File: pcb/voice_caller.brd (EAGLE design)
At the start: 52.4 x 59.1 mm, 48 parts, among them IC1 PRO_MICRO, IC2 LM386M-1, IC3 78L12SMD, K1 TQ2SA-L2-5V, U1 25F32006WSOI

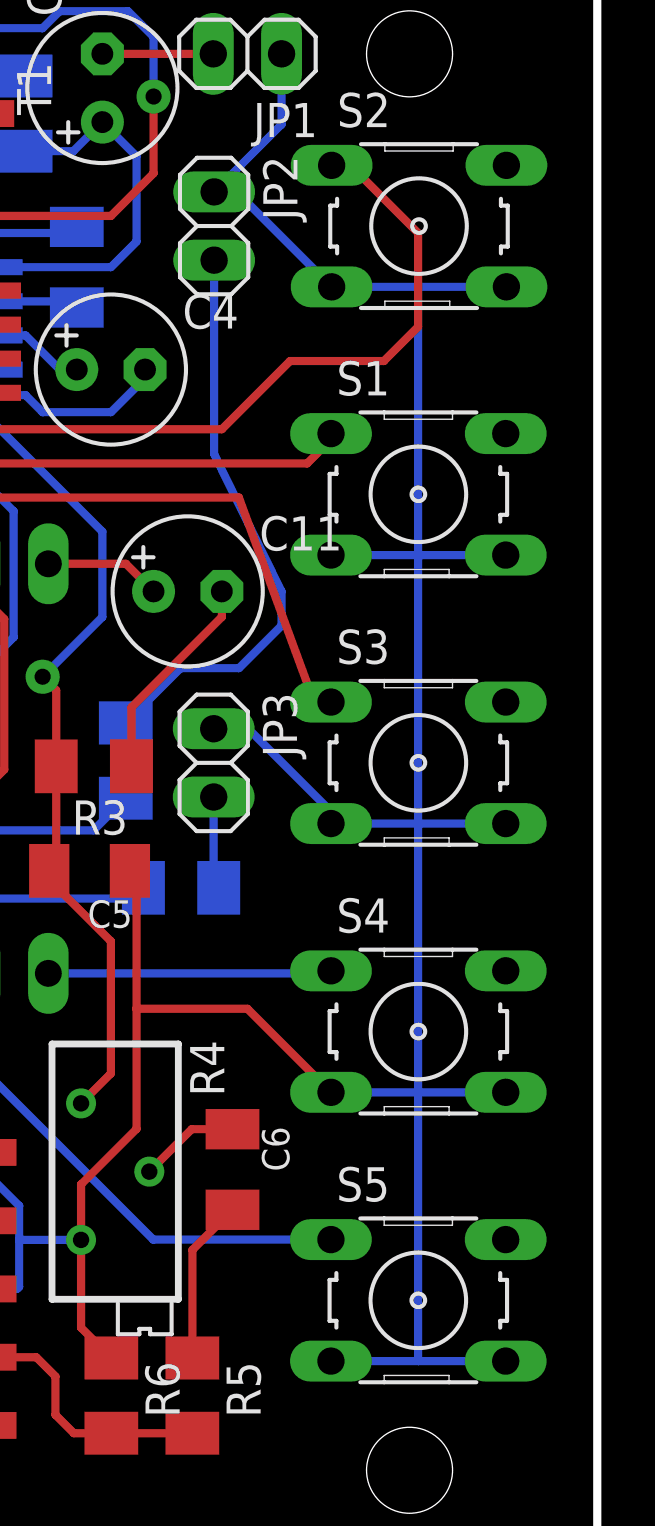
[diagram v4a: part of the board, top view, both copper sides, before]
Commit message: Filter capacitors added to pushbuttons
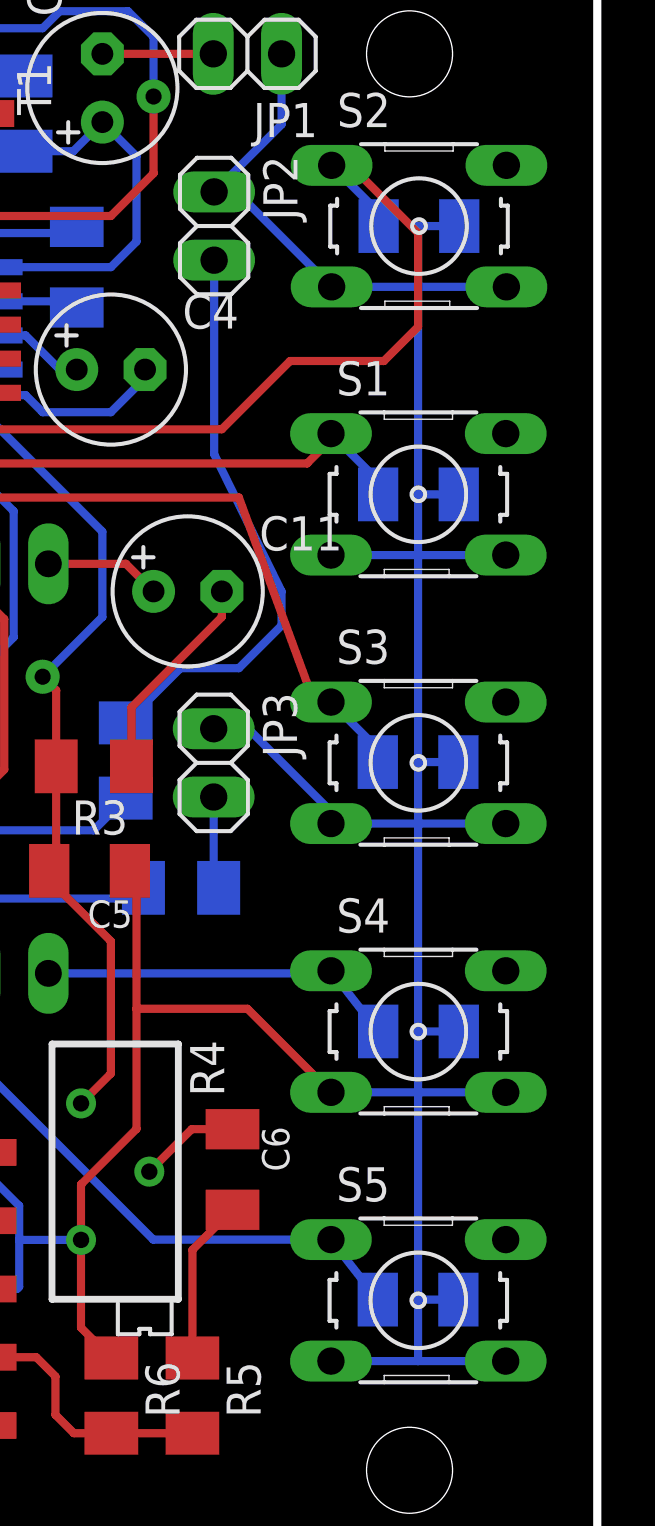
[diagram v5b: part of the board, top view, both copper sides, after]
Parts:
- added C13, C14, C15, C16, C17: 10nF, rcl:C1206K
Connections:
- net BUTTON1: now also C16.1
- net BUTTON2: now also C17.1
- net BUTTON3: now also C13.1
- net BUTTON4: now also C14.1
- net BUTTON5: now also C15.1
- net GND: now also C13.2, C14.2, C15.2, C16.2, C17.2
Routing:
- net GND: track 320.6 -> 330.5 mm
- net BUTTON2: track 29.2 -> 32.2 mm
- net BUTTON1: track 43.8 -> 46.8 mm
- net BUTTON3: track 28.0 -> 31.0 mm
- net BUTTON4: track 10.6 -> 13.4 mm
- net BUTTON5: track 19.2 -> 22.0 mm
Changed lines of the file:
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@@
 <element name="C12" library="rcl" package="C1206K" value="100nF" x="31.115" y="36.5125" rot="MR180"/>
 <element name="D1" library="diode" package="SOD80C" value="" x="30.1625" y="39.37" rot="MR180"/>
+<element name="C13" library="rcl" package="C1206K" value="10nF" x="56.1975" y="35.2425" rot="MR180"/>
+<element name="C14" library="rcl" package="C1206K" value="10nF" x="56.21264375" y="25.218809375" rot="MR180"/>
+<element name="C15" library="rcl" package="C1206K" value="10nF" x="56.1975" y="15.24" rot="MR180"/>
+<element name="C16" library="rcl" package="C1206K" value="10nF" x="56.22905" y="55.187159375" rot="MR180"/>
+<element name="C17" library="rcl" package="C1206K" value="10nF" x="56.21109375" y="45.2026625" rot="MR180"/>
 </elements>
 <signals>
@@
 <wire x1="45.72" y1="21.59" x2="43.65625" y2="19.52625" width="0.3048" layer="1"/>
 <wire x1="43.65625" y1="19.52625" x2="43.65625" y2="17.4625" width="0.3048" layer="1"/>
-<wire x1="56.1975" y1="52.925025" x2="56.1975" y2="42.943775" width="0.3048" layer="16"/>
-<wire x1="56.1975" y1="42.943775" x2="56.1975" y2="32.953740625" width="0.3048" layer="16"/>
-<wire x1="56.1975" y1="32.953740625" x2="56.1975" y2="22.953740625" width="0.3048" layer="16"/>
-<wire x1="56.1975" y1="22.953740625" x2="56.1975" y2="12.95254375" width="0.3048" layer="16"/>
+<wire x1="56.1975" y1="52.925025" x2="56.1975" y2="45.085" width="0.3048" layer="16"/>
+<wire x1="56.1975" y1="45.085" x2="56.1975" y2="42.943775" width="0.3048" layer="16"/>
+<wire x1="56.1975" y1="42.943775" x2="56.1975" y2="35.2425" width="0.3048" layer="16"/>
+<wire x1="56.1975" y1="35.2425" x2="56.1975" y2="32.953740625" width="0.3048" layer="16"/>
+<wire x1="56.1975" y1="32.953740625" x2="56.1975" y2="25.218809375" width="0.3048" layer="16"/>
+<wire x1="56.1975" y1="25.218809375" x2="56.1975" y2="22.953740625" width="0.3048" layer="16"/>
+<wire x1="56.1975" y1="22.953740625" x2="56.1975" y2="15.24" width="0.3048" layer="16"/>
+<wire x1="56.1975" y1="15.24" x2="56.1975" y2="12.95254375" width="0.3048" layer="16"/>
 <wire x1="30.8375" y1="49.2525" x2="30.8375" y2="49.38875" width="0.4064" layer="1"/>
 <wire x1="28.11625" y1="49.38875" x2="30.8375" y2="49.38875" width="0.3048" layer="1"/>
@@
 <wire x1="29.615" y1="36.5125" x2="28.4625" y2="37.665" width="0.3048" layer="16"/>
 <wire x1="28.4625" y1="37.665" x2="28.4625" y2="39.37" width="0.3048" layer="16"/>
+<contactref element="C13" pad="2"/>
+<contactref element="C14" pad="2"/>
+<contactref element="C15" pad="2"/>
+<contactref element="C16" pad="2"/>
+<contactref element="C17" pad="2"/>
+<wire x1="57.71109375" y1="45.2026625" x2="56.3151625" y2="45.2026625" width="0.3048" layer="16"/>
+<wire x1="56.3151625" y1="45.2026625" x2="56.1975" y2="45.085" width="0.3048" layer="16"/>
+<wire x1="57.6975" y1="35.2425" x2="56.1975" y2="35.2425" width="0.3048" layer="16"/>
+<wire x1="57.72905" y1="55.187159375" x2="56.1975" y2="55.187159375" width="0.3048" layer="16"/>
+<wire x1="56.1975" y1="55.187159375" x2="56.1975" y2="52.925025" width="0.3048" layer="16"/>
+<wire x1="57.71264375" y1="25.218809375" x2="56.1975" y2="25.218809375" width="0.3048" layer="16"/>
+<wire x1="57.6975" y1="15.24" x2="56.1975" y2="15.24" width="0.3048" layer="16"/>
 </signal>
 <signal name="MOSI">
@@
 <wire x1="27.2" y1="42.62" x2="27.2" y2="44.345" width="0.3048" layer="1"/>
 <wire x1="27.2" y1="44.345" x2="29.21" y2="46.355" width="0.3048" layer="1"/>
+<contactref element="C17" pad="1"/>
+<wire x1="54.71109375" y1="45.2026625" x2="54.71109375" y2="45.71143125" width="0.3048" layer="16"/>
+<wire x1="54.71109375" y1="45.71143125" x2="52.95755" y2="47.464975" width="0.3048" layer="16"/>
 </signal>
 <signal name="BUTTON1">
@@
 <wire x1="53.6575" y1="57.4675" x2="53.002575" y2="57.4675" width="0.3048" layer="1"/>
 <wire x1="53.002575" y1="57.4675" x2="52.9813" y2="57.446225" width="0.3048" layer="1"/>
+<contactref element="C16" pad="1"/>
+<wire x1="54.72905" y1="55.187159375" x2="54.72905" y2="55.698475" width="0.3048" layer="16"/>
+<wire x1="54.72905" y1="55.698475" x2="52.9813" y2="57.446225" width="0.3048" layer="16"/>
 </signal>
 <signal name="PTT_SENSE">
@@
 <wire x1="52.332175" y1="37.465" x2="52.94729375" y2="37.465" width="0.3048" layer="1"/>
 <wire x1="52.94729375" y1="37.465" x2="52.957234375" y2="37.474940625" width="0.3048" layer="1"/>
+<contactref element="C13" pad="1"/>
+<wire x1="54.6975" y1="35.2425" x2="54.6975" y2="35.734675" width="0.3048" layer="16"/>
+<wire x1="54.6975" y1="35.734675" x2="52.957234375" y2="37.474940625" width="0.3048" layer="16"/>
 </signal>
 <signal name="BUTTON5">
@@
 <wire x1="46.34375625" y1="17.47374375" x2="39.9" y2="23.9175" width="0.3048" layer="16"/>
 <wire x1="39.9" y1="23.9175" x2="39.9" y2="27.38" width="0.3048" layer="16"/>
+<contactref element="C15" pad="1"/>
+<wire x1="54.6975" y1="15.24" x2="52.954765625" y2="17.47374375" width="0.3048" layer="16"/>
 </signal>
 <signal name="BUTTON4">
@@
 <wire x1="42.44" y1="27.38" x2="52.86229375" y2="27.38" width="0.3048" layer="16"/>
 <wire x1="52.86229375" y1="27.38" x2="52.957234375" y2="27.474940625" width="0.3048" layer="16"/>
+<contactref element="C14" pad="1"/>
+<wire x1="54.71264375" y1="25.218809375" x2="52.957234375" y2="27.474940625" width="0.3048" layer="16"/>
 </signal>
 <signal name="PTT_SW">

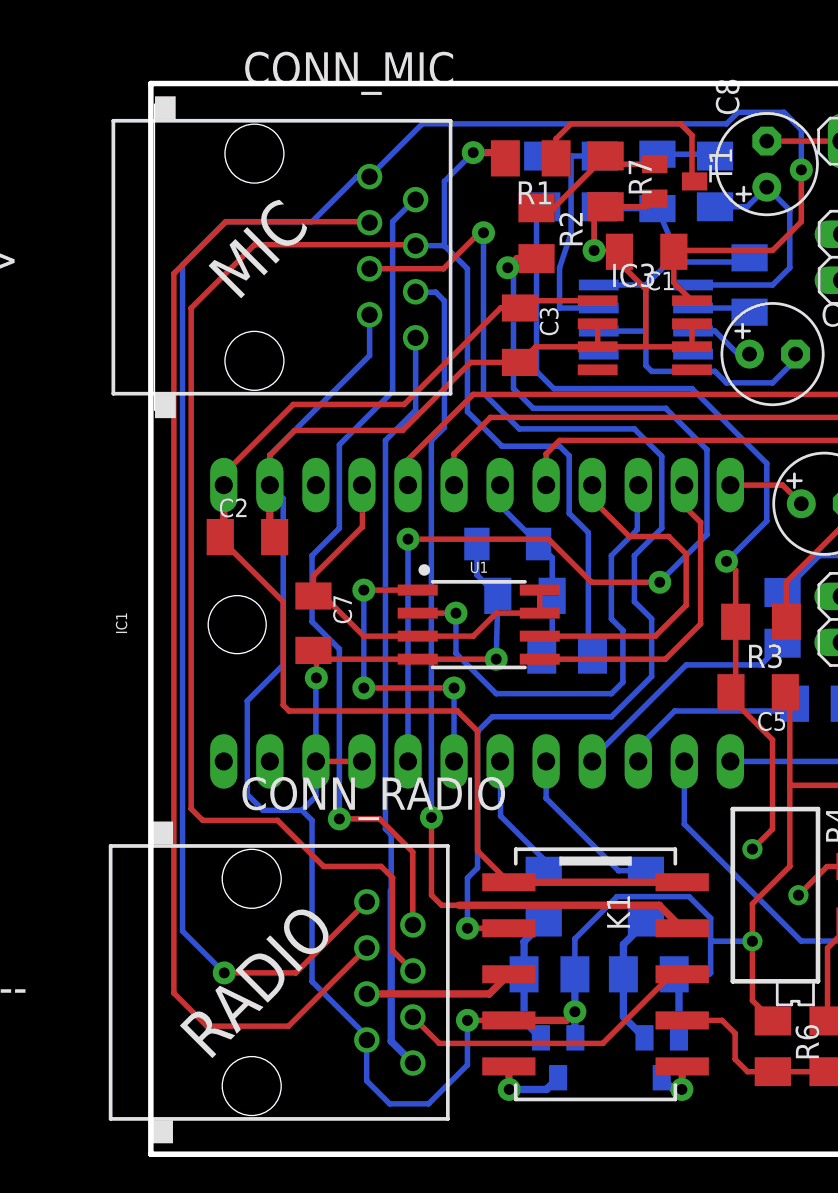
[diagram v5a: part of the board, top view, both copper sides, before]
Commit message: RJ-45 connectors moves 1.3mm inwards.
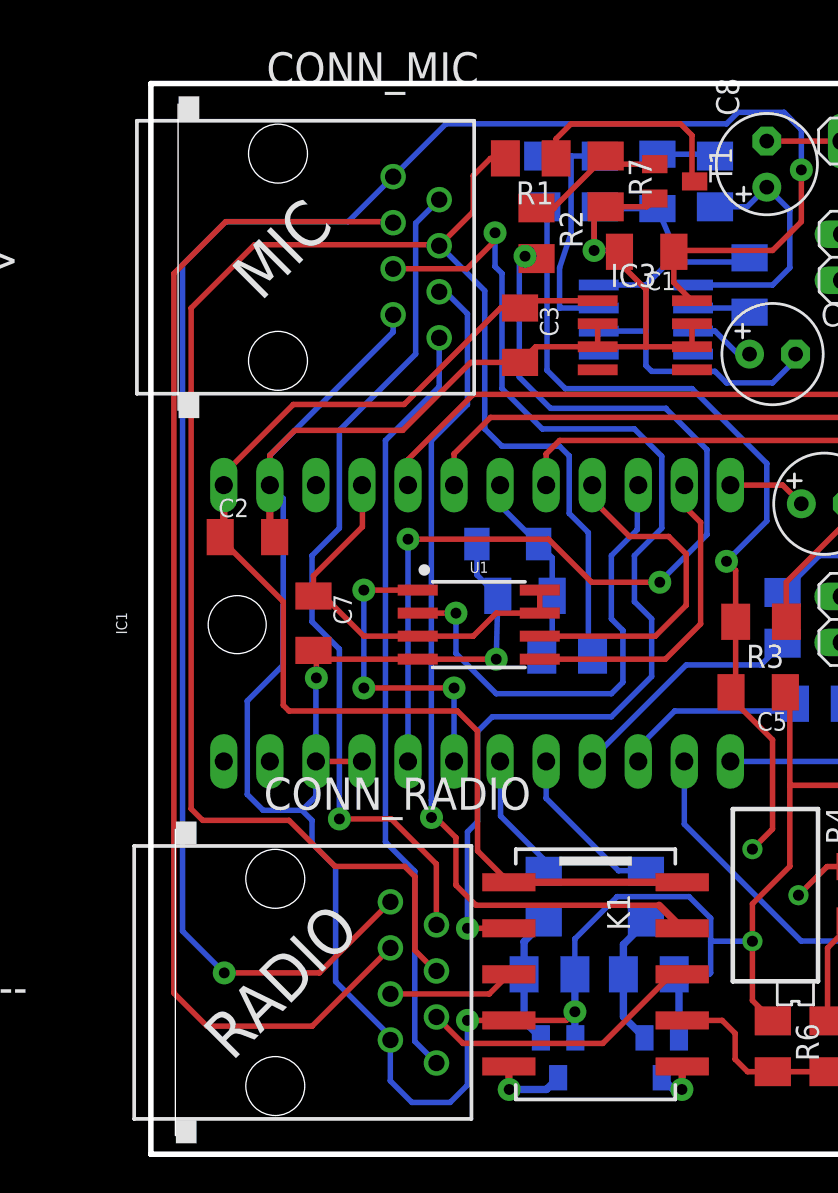
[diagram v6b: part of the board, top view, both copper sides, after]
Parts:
- moved CONN_RADIO 1.30 mm to (17.3, 15.2)
- moved CONN_MIC 1.30 mm to (17.5, 55.2)
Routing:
- net AF_OUT: track 64.9 -> 67.5 mm
- net FREQ_UD: track 46.0 -> 47.4 mm
- net MIC_GND: track 64.6 -> 63.2 mm
- net +8V: track 103.4 -> 104.7 mm
- net MIC_RADIO: track 17.0 -> 15.7 mm
- net MIC_GND_RADIO: track 8.28 -> 6.98 mm
- net PTT_SW: track 56.2 -> 55.1 mm
- net SQUELCH: track 41.3 -> 42.4 mm
- net MIC: track 49.5 -> 48.6 mm
- net PTT: track 96.9 -> 97.6 mm, vias 1 -> 0

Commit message: Final adjustments.
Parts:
- removed JP1, JP2, JP3: (no value), pinhead:1X02
- removed K1: TQ2SA-L2-5V, relay:TQ-SA
- removed U1: 25F32006WSOI, SparkFun-IC-Memory:SO08-EIAJ
- added ARDUINO: PRO_MICRO, SparkFun-Boards:SPARKFUN_PRO_MICRO
- added LED1, LED2, SPK: (no value), pinhead:1X02
- added RLY1: TQ2SA-L2-5V, relay:TQ-SA
- IC1: value PRO_MICRO -> 78L12SMD; device SparkFun-Boards:SPARKFUN_PRO_MICRO -> linear:SO08
- IC3: value 78L12SMD -> 25F32006WSOI; device linear:SO08 -> SparkFun-IC-Memory:SO08-EIAJ
- moved IC3 56.4 mm to (13.3, 0.00)
- moved S2 47.8 mm to (40.6, 9.96)
- moved C16 38.5 mm to (40.6, 19.9)
- moved C14 38.5 mm to (40.6, -10.0)
- moved C17 38.5 mm to (40.6, 9.96)
- moved S3 38.5 mm to (40.6, -0.03)
- moved S4 38.5 mm to (40.6, -10.0)
- moved S5 38.5 mm to (40.6, -20.0)
- moved C13 38.5 mm to (40.6, 0.00)
- moved C15 38.5 mm to (40.6, -20.0)
- moved CONN_MIC 38.4 mm to (2.00, 20.0)
- moved CONN_RADIO 38.4 mm to (2.00, -20.0)
- moved C10 38.1 mm to (28.3, 18.7)
- moved C11 38.1 mm to (32.4, 6.67)
- moved C12 38.1 mm to (15.9, 1.59)
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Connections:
- net +3V3: now also ARDUINO.21, IC3.3, IC3.7, IC3.8; no longer IC1.21, U1.3, U1.7, U1.8
- net +5V: now also ARDUINO.24, IC1.1, RLY1.1, RLY1.10; no longer IC1.24, IC3.1, K1.1, K1.10
- net +8V: now also IC1.8; no longer IC3.8
- net BUTTON1: now also ARDUINO.20, S1.1; no longer IC1.20, S2.1
- net BUTTON2: now also ARDUINO.19, S2.1; no longer IC1.19, S1.1
- net BUTTON3: now also ARDUINO.17; no longer IC1.17
- net BUTTON4: now also ARDUINO.12; no longer IC1.12
- net BUTTON5: now also ARDUINO.11; no longer IC1.11
- net FLASH_CS: now also ARDUINO.6, IC3.1; no longer IC1.6, U1.1
- net GND: now also ARDUINO.23, ARDUINO.3, ARDUINO.4, IC1.2, IC1.6, IC1.7, IC3.4, LED1.1, LED2.1, RLY1.4, SPK.1; no longer IC1.23, IC1.4, IC3.2, IC3.3, IC3.6, IC3.7, JP1.1, JP2.1, JP3.1, K1.4, U1.4
- net MIC: now also RLY1.9; no longer K1.9
- net MIC_GND: now also RLY1.2; no longer K1.2
- net MIC_GND_RADIO: now also RLY1.3; no longer K1.3
- net MIC_PWM: now also RLY1.7; no longer K1.7
- net MIC_RADIO: now also RLY1.8; no longer K1.8
- net MISO: now also ARDUINO.15, IC3.2; no longer IC1.15, U1.2
- net MOSI: now also ARDUINO.14, IC3.5; no longer IC1.14, U1.5
- net N$10: now also RLY1.5; no longer K1.5
- net N$12: now also ARDUINO.9; no longer IC1.9
- net N$13: now also RLY1.6; no longer K1.6
- net N$15: now also ARDUINO.10; no longer IC1.10
- net N$22: now also SPK.2; no longer JP1.2
- net N$4: now also LED2.2; no longer JP2.2
- net N$9: now also LED1.2; no longer JP3.2
- net PTT_SENSE: now also ARDUINO.18; no longer IC1.18
- net PTT_SW: now also ARDUINO.5; no longer IC1.5
- net PULSE_RX: now also ARDUINO.8; no longer IC1.8
- net PULSE_TX: now also ARDUINO.7; no longer IC1.7
- net PWM: now also ARDUINO.13; no longer IC1.13
- net SCK: now also ARDUINO.16, IC3.6; no longer IC1.16, U1.6
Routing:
- net GND: track 330.9 -> 335.8 mm
- net BUTTON3: track 31.0 -> 31.9 mm
- net BUTTON1: track 46.8 -> 47.7 mm
- net MIC_GND_RADIO: track 6.98 -> 7.83 mm
- net MIC: track 48.6 -> 49.3 mm
- net MIC_GND: track 63.2 -> 63.9 mm
- net AF_OUT: track 67.5 -> 66.8 mm
- net +5V: track 69.1 -> 69.8 mm
- net PULSE_RX: track 9.20 -> 9.84 mm
- net MIC_PWM: track 10.0 -> 9.39 mm
- net MIC_RADIO: track 15.7 -> 16.3 mm
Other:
- board size 52.4 x 59.1 mm -> 52.4 x 63.1 mm
- board text removed: "MIC -->"
- board text removed: "RADIO <--"

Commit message: AF amp attenuator changed.
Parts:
- R15: value 220 -> 22k
- R16: value 220 -> 220 x 100pF
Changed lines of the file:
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@@
 <attribute name="VALUE" x="26.1575" y="17.1325" size="1.016" layer="28" rot="MR90"/>
 </element>
-<element name="R15" library="rcl" package="M1206" value="220" x="16.8275" y="24.4475" smashed="yes" rot="MR270">
+<element name="R15" library="rcl" package="M1206" value="22k" x="16.8275" y="24.4475" smashed="yes" rot="MR270">
 <attribute name="NAME" x="17.145" y="27.6225" size="1.016" layer="26" rot="MR0"/>
 <attribute name="VALUE" x="19.3675" y="25.7175" size="1.27" layer="28" rot="MR270"/>
 </element>
-<element name="R16" library="rcl" package="M1206" value="220" x="20.0025" y="24.4475" smashed="yes" rot="MR90">
+<element name="R16" library="rcl" package="M1206" value="220 x 100pF" x="20.0025" y="24.4475" smashed="yes" rot="MR90">
 <attribute name="NAME" x="21.59" y="27.6225" size="1.016" layer="26" rot="MR0"/>
 <attribute name="VALUE" x="17.4625" y="23.1775" size="1.27" layer="28" rot="MR90"/>
